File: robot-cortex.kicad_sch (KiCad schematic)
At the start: 6 parts, among them Q1 NPN, Q2 NPN, U1 CP2102N-A02-GQFN20R

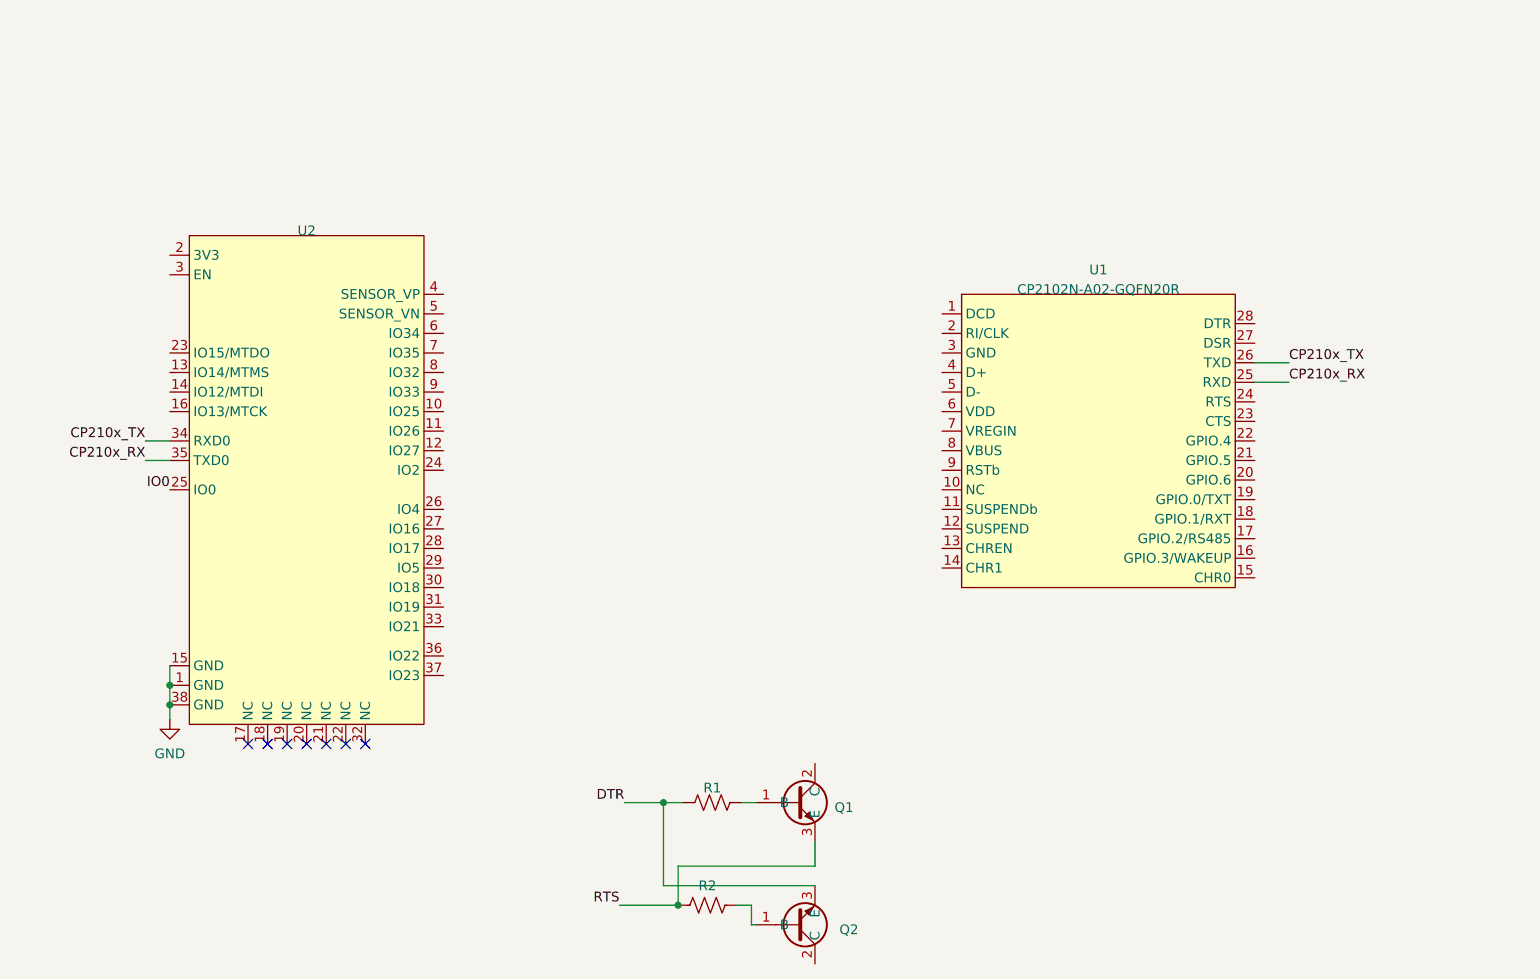
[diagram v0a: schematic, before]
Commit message: added 3dmodels and updated esp32 footprint
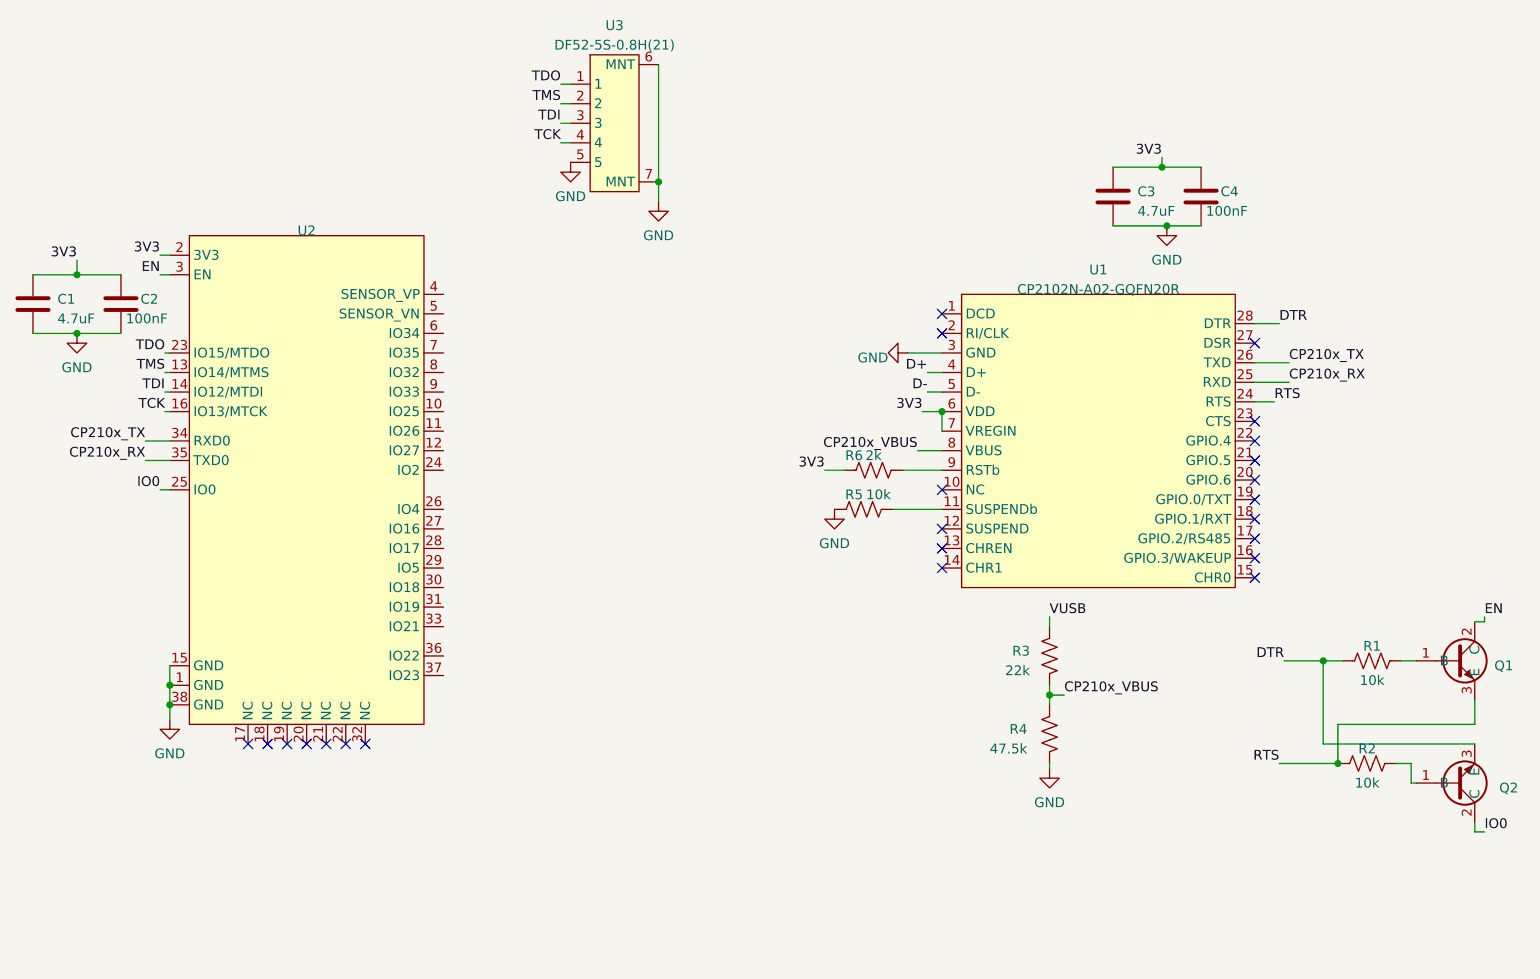
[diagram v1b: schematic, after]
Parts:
- added C1, C3: 4.7uF, robot-cortex:C_0603_1608Metric, symbol robot-cortex:Capacitor
- added C2, C4: 100nF, robot-cortex:C_0402_1005Metric, symbol robot-cortex:Capacitor
- added R3: 22k, robot-cortex:R_0402_1005Metric, symbol robot-cortex:Resistor
- added R4: 47.5k, robot-cortex:R_0402_1005Metric, symbol robot-cortex:Resistor
- added R5: 10k, robot-cortex:R_0402_1005Metric, symbol robot-cortex:Resistor
- added R6: 2k, robot-cortex:R_0402_1005Metric, symbol robot-cortex:Resistor
- added U3: DF52-5S-0.8H(21), robot-cortex:DF52-5S-0.8H(21), symbol robot-cortex:DF52-5S-0.8H(21)
- R1, R2: value Resistor -> 10k; footprint (none) -> robot-cortex:R_0402_1005Metric
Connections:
- net DTR: now also U1.28 (DTR)
- net GND: now also U1.3 (GND), C1.2, C2.2, C3.2, C4.2, R4.1, R5.2, U3.5, U3.6 (MNT), U3.7 (MNT)
- net IO0: now also Q2.2 (C)
- net RTS: now also U1.24 (RTS)
- net EN: now reaches Q1.2 (C)
- net EN: now also U2.3 (EN)
- net TMS: now reaches U2.13 (IO14/MTMS)
- net TMS: now also U3.2
- net TDI: now reaches U2.14 (IO12/MTDI)
- net TDI: now also U3.3
- net TCK: now reaches U2.16 (IO13/MTCK)
- net TCK: now also U3.4
- net 3V3: now reaches U2.2 (3V3)
- net 3V3: now also U1.6 (VDD), U1.7 (VREGIN), C1.1, C2.1, C3.1, C4.1, R6.2
- net TDO: now reaches U2.23 (IO15/MTDO)
- net TDO: now also U3.1
- net at U1.11 (SUSPENDb): now also R5.1
- net D+: now reaches U1.4 (D+)
- net D-: now reaches U1.5 (D-)
- net CP210x_VBUS: now reaches U1.8 (VBUS)
- net CP210x_VBUS: now also R3.1, R4.2
- net at U1.9 (RSTb): now also R6.1
- new net VUSB: R3.2
- no-connect marks 7 -> 23
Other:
- moved on the sheet: Q1, Q2, R1

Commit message: updated value field
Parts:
- U2: value ~ -> ESP32-WROOM-32E-H4
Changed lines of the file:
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@@
   )
   (symbol (lib_id "robot-cortex:ESP32-WROOM-32E-H4") (at 51.435 76.835 0) (unit 1)
-    (in_bom yes) (on_board yes) (dnp no) (fields_autoplaced)
+    (in_bom yes) (on_board yes) (dnp no)
     (property "Reference" "U2" (at 51.435 39.37 0)
       (effects (font (size 1.27 1.27)))
     )
-    (property "Value" "~" (at 40.005 74.295 0)
+    (property "Value" "ESP32-WROOM-32E-H4" (at 49.53 80.645 0)
       (effects (font (size 1.27 1.27)))
     )

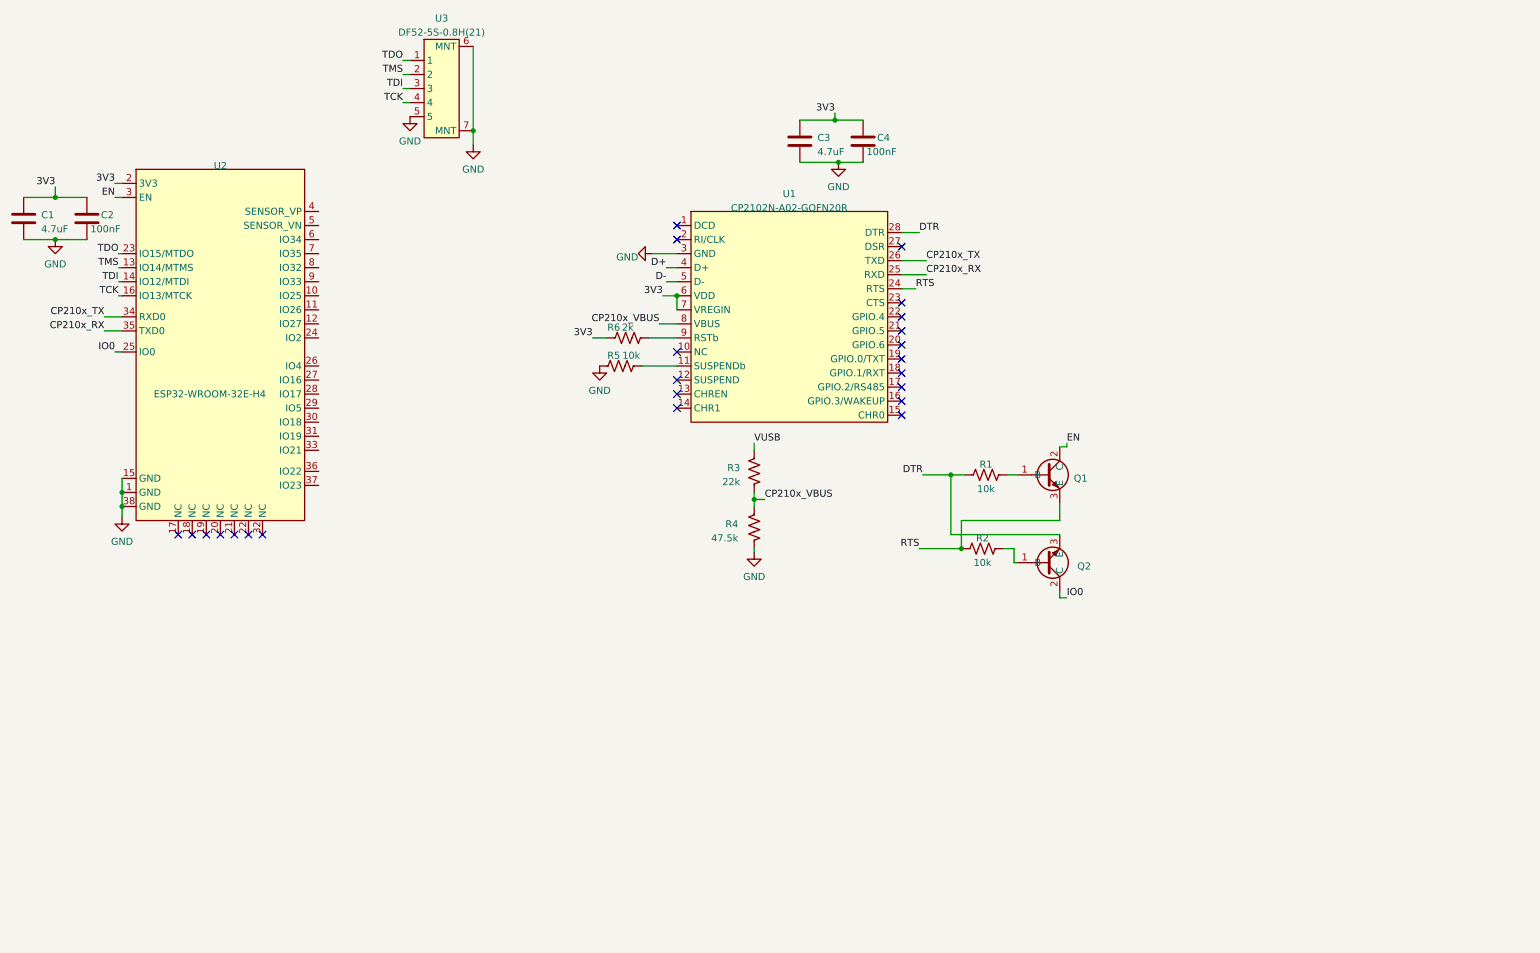
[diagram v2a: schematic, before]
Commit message: added many components
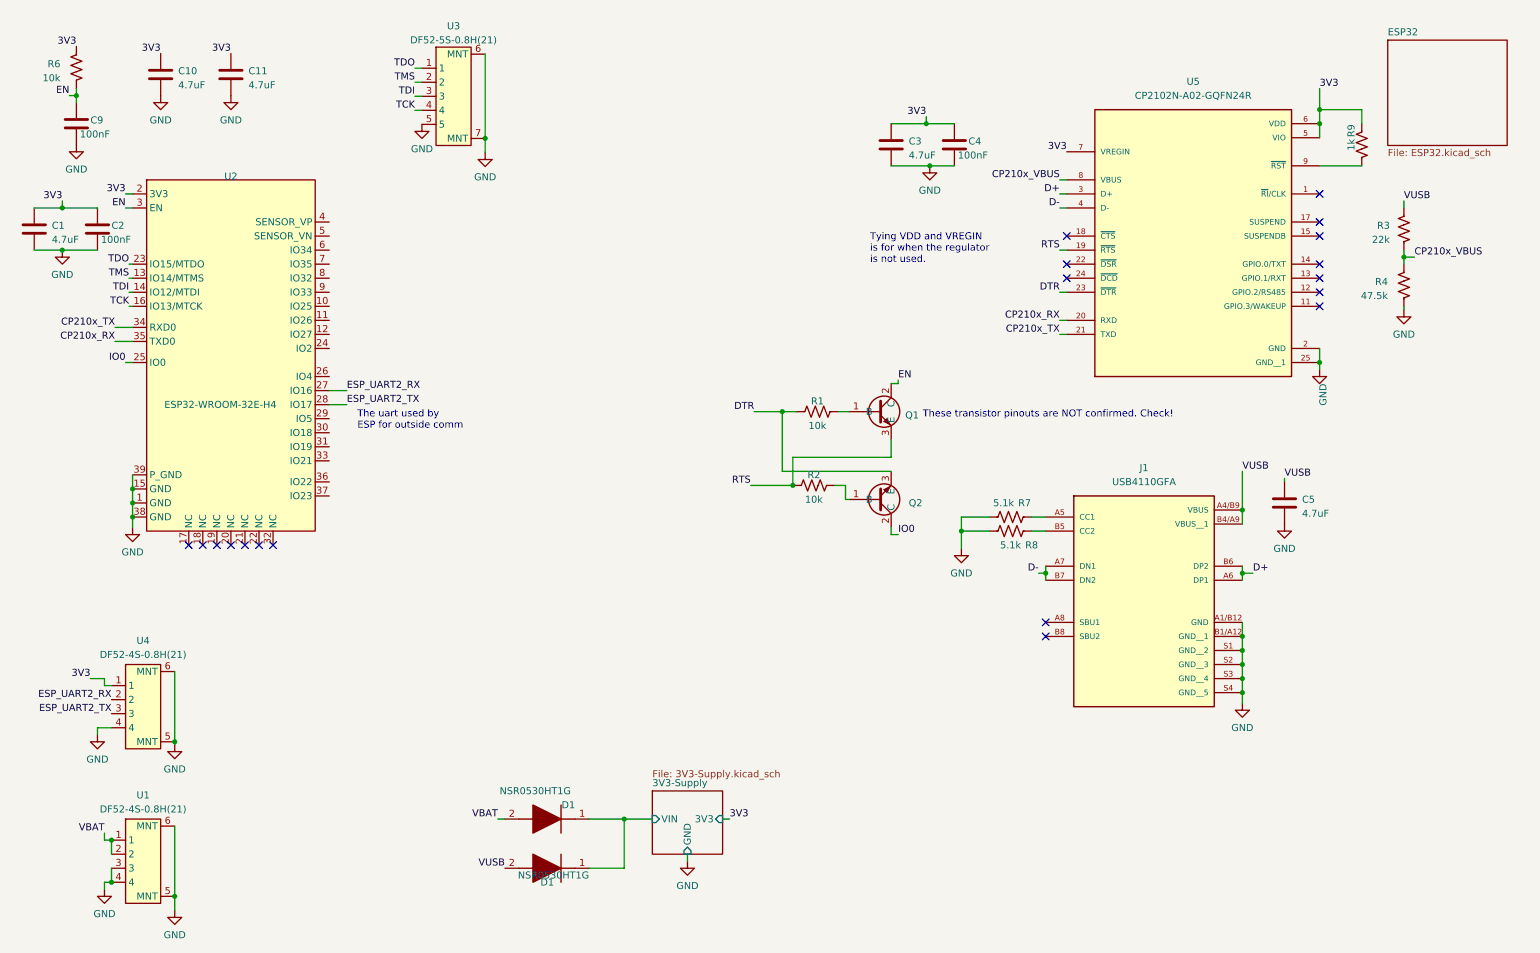
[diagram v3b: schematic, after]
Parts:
- removed R5: 10k, robot-cortex:R_0402_1005Metric, symbol robot-cortex:Resistor
- removed U1: CP2102N-A02-GQFN20R, symbol robot-cortex:CP2102N-A02-GQFN20R
- added C10, C11, C5: 4.7uF, robot-cortex:C_0603_1608Metric, symbol robot-cortex:Capacitor
- added C9: 100nF, robot-cortex:C_0402_1005Metric, symbol robot-cortex:Capacitor
- added D1 (x2): NSR0530HT1G, robot-cortex:SOD2512X110N, symbol SamacSys_Parts:NSR0530HT1G
- added J1: USB4110GFA, robot-cortex:GCT_USB4110GFA, symbol robot-cortex:USB4110GFA
- added R7, R8: 5.1k, robot-cortex:R_0402_1005Metric, symbol NeuralStimulatorAndRecorder:Resistor
- added R9: 1k, robot-cortex:R_0402_1005Metric, symbol robot-cortex:Resistor
- added U1, U4: DF52-4S-0.8H(21), robot-cortex:DF52-4S-0.8H(21), symbol robot-cortex:DF52-4S-0.8H(21)
- added U5: CP2102N-A02-GQFN24R, robot-cortex:QFN50P400X400X80-25N, symbol robot-cortex:CP2102N-A02-GQFN24R
- Q1, Q2: footprint (none) -> robot-cortex:SOT-23-3
- R6: value 2k -> 10k
- U2: footprint (none) -> robot-cortex:ESP32-WROOM-32
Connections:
- net 3V3: now also C10.1, C11.1, R9.2, U4.1, U5.5 (VIO), U5.6 (VDD), U5.7 (VREGIN)
- net CP210x_RX: now also U5.20 (RXD)
- net CP210x_TX: now also U5.21 (TXD)
- net CP210x_VBUS: now also U5.8 (VBUS)
- net D+: now also J1.A6 (DP1), J1.B6 (DP2), U5.3 (D+)
- net D-: now also J1.A7 (DN1), J1.B7 (DN2), U5.4 (D-)
- net DTR: now also U5.23 (~{DTR})
- net EN: now also R6.1, C9.1
- net GND: now also U2.39 (P_GND), C10.2, C11.2, C5.2, C9.2, J1.A1/B12 (GND), J1.B1/A12 (GND__1), J1.S1 (GND__2), J1.S2 (GND__3), J1.S3 (GND__4), J1.S4 (GND__5), R7.1, R8.1, U1.3, U1.4, U1.5 (MNT), U1.6 (MNT), U4.4, U4.5 (MNT), U4.6 (MNT), U5.2 (GND), U5.25 (GND__1)
- net RTS: now also U5.19 (~{RTS})
- net VUSB: now also C5.1, D1.2 (A), J1.A4/B9 (VBUS), J1.B4/A9 (VBUS__1)
- net ESP_UART2_RX: now reaches U2.27 (IO16)
- net ESP_UART2_RX: now also U4.2
- net ESP_UART2_TX: now reaches U2.28 (IO17)
- net ESP_UART2_TX: now also U4.3
- new net: J1.B5 (CC2), R8.2
- new net: R9.1, U5.9 (~{RST})
- new net: J1.A5 (CC1), R7.2
- new net 3V3-Supply/VIN: D1.1 (K), D1.1 (K)
- new net VBAT: D1.2 (A), U1.1, U1.2
- no-connect marks 23 -> 19
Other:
- added sheet 3V3-Supply (3V3-Supply.kicad_sch)
- added sheet ESP32 (ESP32.kicad_sch)
- note added: "The uart used by ESP for outside comm"
- note added: "These transistor pinouts are NOT confirmed. Check!"
- note added: "Tying VDD and VREGIN is for when the regulator is not used."
- moved on the sheet: C1, C2, C3, C4, Q1, Q2, R1, R2, R3, R4, U3

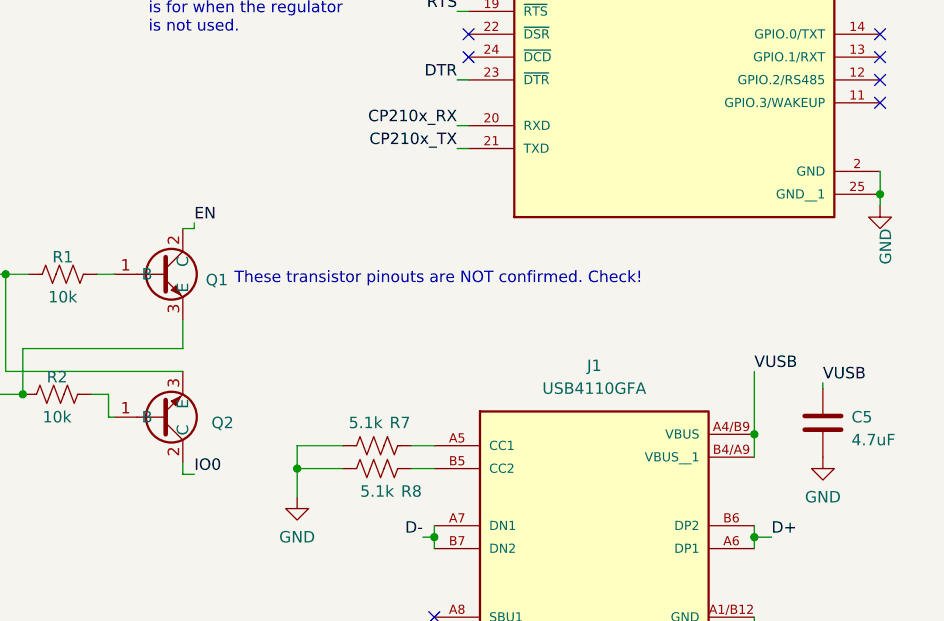
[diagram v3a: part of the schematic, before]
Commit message: checked and fixed npn issue, added mpn
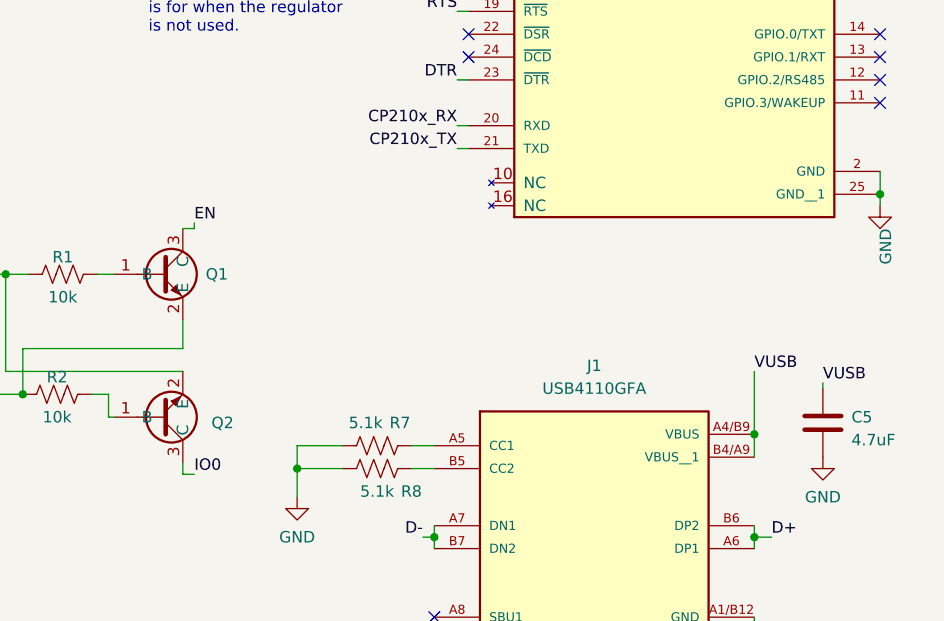
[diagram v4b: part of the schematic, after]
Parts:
- Q1, Q2: value NPN -> SS8050-G; symbol robot-cortex:NPN -> robot-cortex:SS8050-G
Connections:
- net DTR: now also Q2.2 (E); no longer Q2.3 (E)
- net EN: now also Q1.3 (C); no longer Q1.2 (C)
- net IO0: now also Q2.3 (C); no longer Q2.2 (C)
- net RTS: now also Q1.2 (E); no longer Q1.3 (E)
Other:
- note removed: "These transistor pinouts are NOT confirmed. Check!"
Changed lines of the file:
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@@
-    (effects (font (size 1.27 1.27)) (justify left bottom))
-  )
-  (text "These transistor pinouts are NOT confirmed. Check!"
-    (at 178.435 85.09 0)
     (effects (font (size 1.27 1.27)) (justify left bottom))
   )
@@
     )
   )
-  (symbol (lib_id "robot-cortex:NPN") (at 165.1 83.82 0) (unit 1)
-    (in_bom yes) (on_board yes) (dnp no) (fields_autoplaced)
-    (property "Reference" "Q1" (at 175.26 84.455 0)
-      (effects (font (size 1.27 1.27)) (justify left))
-    )
-    (property "Value" "NPN" (at 160.02 76.2 0)
+  (symbol (lib_id "robot-cortex:SS8050-G") (at 165.1 83.82 0) (unit 1)
+    (in_bom yes) (on_board yes) (dnp no) (fields_autoplaced)
+    (property "Reference" "Q1" (at 175.26 83.82 0)
+      (effects (font (size 1.27 1.27)) (justify left))
+    )
+    (property "Value" "SS8050-G" (at 160.02 76.2 0)
       (effects (font (size 1.27 1.27)) hide)
     )
@@
     )
   )
-  (symbol (lib_id "robot-cortex:NPN") (at 165.1 99.695 0) (mirror x) (unit 1)
+  (symbol (lib_id "robot-cortex:SS8050-G") (at 165.1 99.695 0) (mirror x) (unit 1)
     (in_bom yes) (on_board yes) (dnp no)
     (property "Reference" "Q2" (at 175.895 100.33 0)
       (effects (font (size 1.27 1.27)) (justify left))
     )
-    (property "Value" "NPN" (at 160.02 107.315 0)
+    (property "Value" "SS8050-G" (at 160.02 107.315 0)
       (effects (font (size 1.27 1.27)) hide)
     )
@@
     (pin "8")
     (pin "9")
-    (instances
-      (project "robot-cortex"
+    (pin "10")
+    (pin "16")
+    (instances
+      (project "robot-cortex"
